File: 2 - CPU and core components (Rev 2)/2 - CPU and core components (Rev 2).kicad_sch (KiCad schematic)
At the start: 1 part

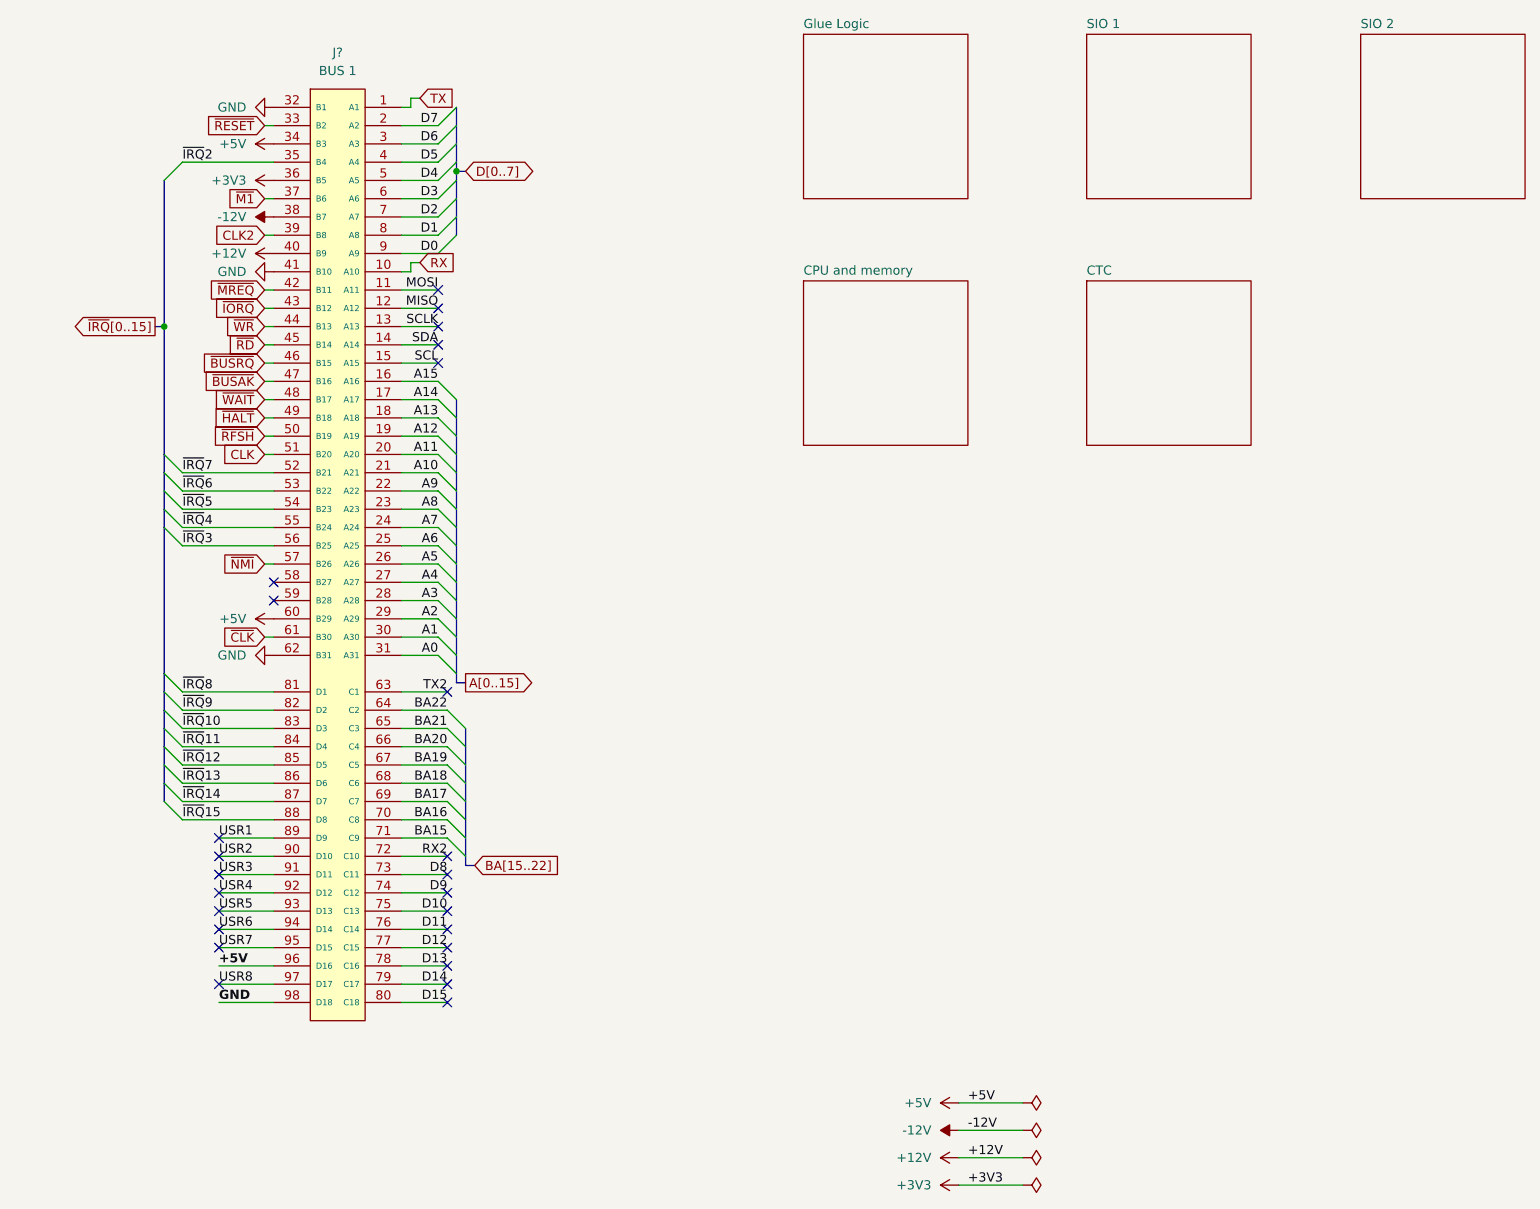
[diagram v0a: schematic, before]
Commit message: Replacing a lot of TTL chips by 2 PLDs. Also, added blinkenlights.
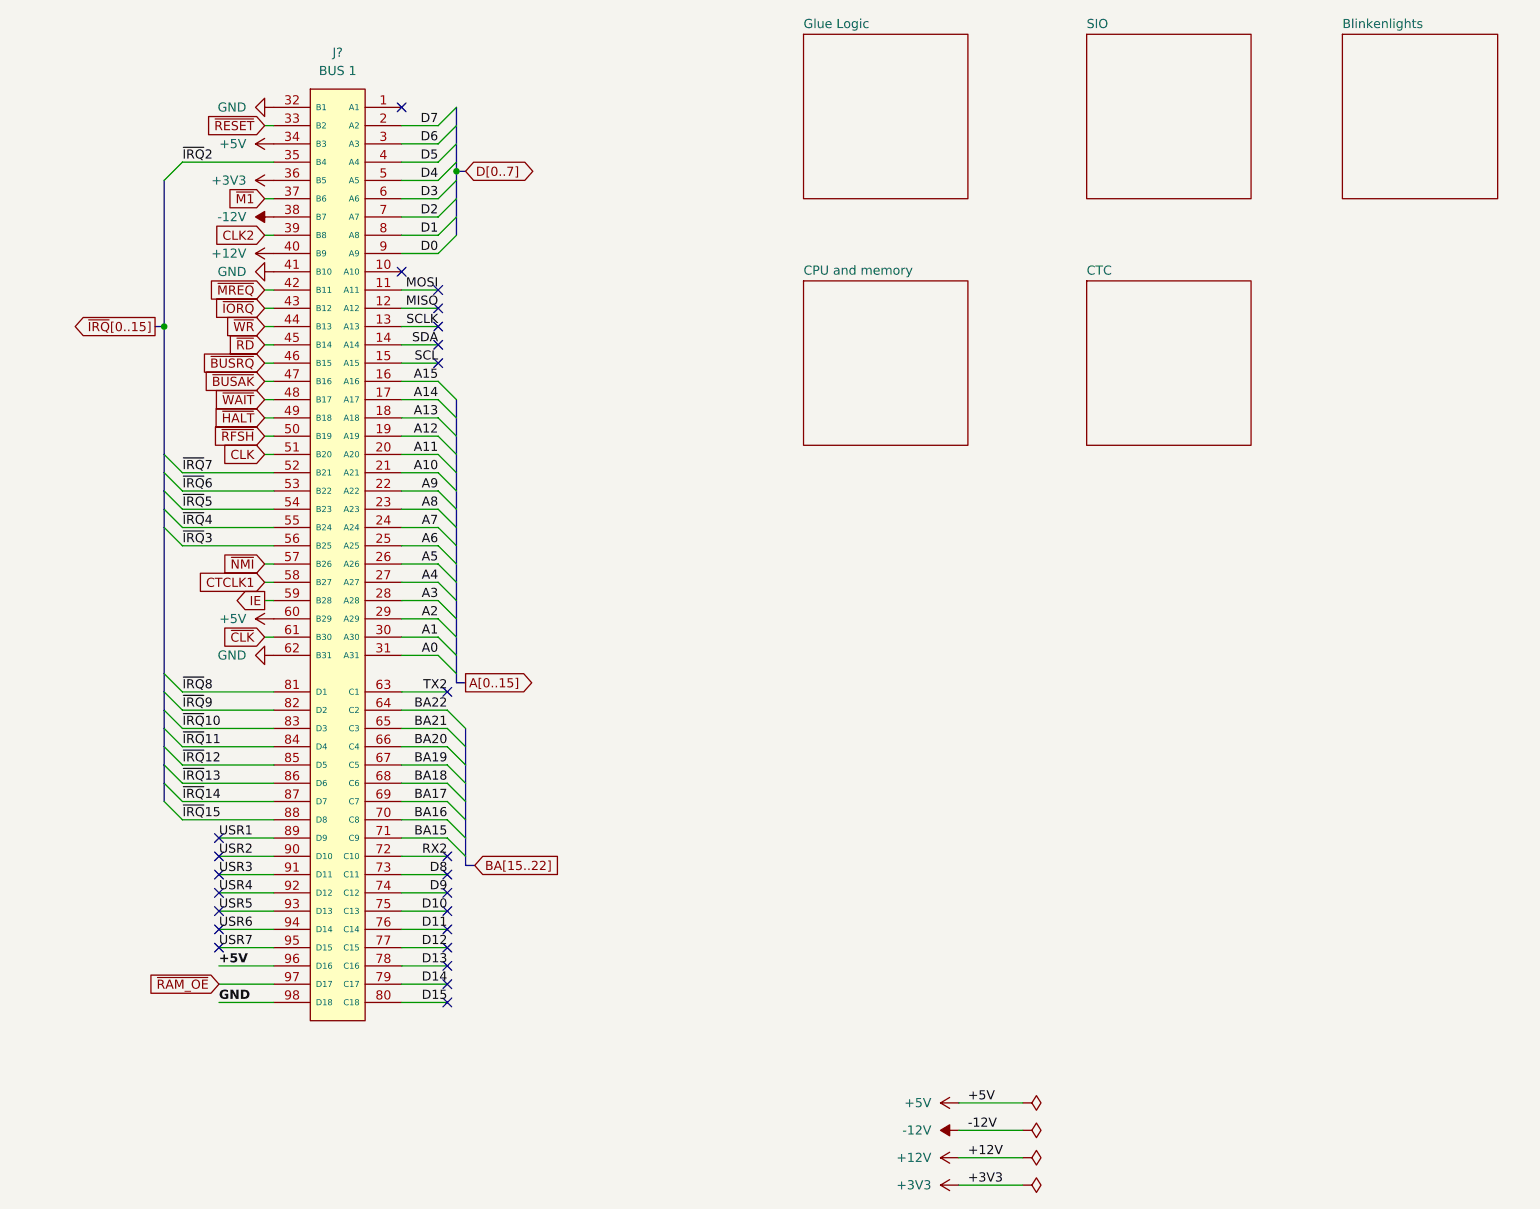
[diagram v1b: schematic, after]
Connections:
- net CTCLK1: now reaches J?.58 (B27)
- net IE: now reaches J?.59 (B28)
- net RX: no longer names the net of J?.10 (A10)
- net TX: no longer names the net of J?.1 (A1)
- net USR8 renamed ~{RAM_OE}
- no-connect marks 25 -> 24
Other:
- sheet SIO 1 renamed SIO
- removed sheet SIO 2
- added sheet Blinkenlights (Blinkenlights.kicad_sch)
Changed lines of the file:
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@@
   )
   (no_connect (at 72.39 152.4))
-  (no_connect (at 48.26 111.76))
   (no_connect (at 40.64 144.78))
   (no_connect (at 71.12 73.66))
@@
   (no_connect (at 40.64 160.02))
   (no_connect (at 40.64 152.4))
-  (no_connect (at 48.26 109.22))
   (no_connect (at 72.39 157.48))
   (no_connect (at 71.12 68.58))
   (no_connect (at 72.39 162.56))
   (no_connect (at 72.39 167.64))
+  (no_connect (at 66.04 66.04))
   (no_connect (at 71.12 76.2))
   (no_connect (at 72.39 165.1))
+  (no_connect (at 66.04 43.18))
   (no_connect (at 40.64 154.94))
   (no_connect (at 40.64 149.86))
-  (no_connect (at 40.64 165.1))
   (no_connect (at 71.12 71.12))
   (no_connect (at 40.64 157.48))
@@
     (stroke (width 0) (type default))
   )
-  (wire (pts (xy 68.58 41.91) (xy 67.31 41.91))
-    (stroke (width 0) (type default))
-  )
   (wire (pts (xy 66.04 106.68) (xy 71.12 106.68))
     (stroke (width 0) (type default))
@@
     (stroke (width 0) (type default))
   )
-  (wire (pts (xy 67.31 66.04) (xy 66.04 66.04))
-    (stroke (width 0) (type default))
-  )
   (bus (pts (xy 73.66 83.82) (xy 73.66 86.36))
     (stroke (width 0) (type default))
@@
     (stroke (width 0) (type default))
   )
-  (wire (pts (xy 67.31 64.77) (xy 68.58 64.77))
-    (stroke (width 0) (type default))
-  )
   (wire (pts (xy 143.51 189.23) (xy 152.4 189.23))
     (stroke (width 0) (type default))
@@
     (stroke (width 0) (type default))
   )
-  (wire (pts (xy 67.31 64.77) (xy 67.31 66.04))
+  (wire (pts (xy 46.99 111.76) (xy 48.26 111.76))
     (stroke (width 0) (type default))
   )
@@
     (stroke (width 0) (type default))
   )
-  (wire (pts (xy 67.31 41.91) (xy 67.31 43.18))
-    (stroke (width 0) (type default))
-  )
   (wire (pts (xy 40.64 154.94) (xy 48.26 154.94))
     (stroke (width 0) (type default))
@@
     (stroke (width 0) (type default))
   )
+  (wire (pts (xy 46.99 109.22) (xy 48.26 109.22))
+    (stroke (width 0) (type default))
+  )
   (bus (pts (xy 33.02 96.52) (xy 33.02 99.06))
     (stroke (width 0) (type default))
@@
   )
   (bus (pts (xy 33.02 99.06) (xy 33.02 101.6))
-    (stroke (width 0) (type default))
-  )
-  (wire (pts (xy 66.04 43.18) (xy 67.31 43.18))
     (stroke (width 0) (type default))
   )
@@
     (effects (font (size 1.27 1.27)) (justify right bottom))
   )
-  (label "USR8" (at 40.64 165.1 0) (fields_autoplaced)
-    (effects (font (size 1.27 1.27)) (justify left bottom))
-  )
   (label "GND" (at 40.64 167.64 0) (fields_autoplaced)
     (effects (font (size 1.27 1.27) (thickness 0.254) bold) (justify left bottom))
@@
     )
   )
-  (global_label "TX" (shape input) (at 68.58 41.91 0) (fields_autoplaced)
-    (effects (font (size 1.27 1.27)) (justify left))
-    (property "Intersheetrefs" "${INTERSHEET_REFS}" (at 73.7423 41.91 0)
-      (effects (font (size 1.27 1.27)) (justify left) hide)
-    )
-  )
   (global_label "CLK2" (shape input) (at 46.99 60.96 180) (fields_autoplaced)
     (effects (font (size 1.27 1.27)) (justify right))
     (property "Intersheetrefs" "${INTERSHEET_REFS}" (at 39.2272 60.96 0)
       (effects (font (size 1.27 1.27)) (justify right) hide)
-    )
-  )
-  (global_label "RX" (shape input) (at 68.58 64.77 0) (fields_autoplaced)
-    (effects (font (size 1.27 1.27)) (justify left))
-    (property "Intersheetrefs" "${INTERSHEET_REFS}" (at 74.0447 64.77 0)
-      (effects (font (size 1.27 1.27)) (justify left) hide)
     )
   )
@@
     )
   )
+  (global_label "CTCLK1" (shape input) (at 46.99 109.22 180) (fields_autoplaced)
+    (effects (font (size 1.27 1.27)) (justify right))
+    (property "Intersheetrefs" "${INTERSHEET_REFS}" (at 36.9896 109.22 0)
+      (effects (font (size 1.27 1.27)) (justify right) hide)
+    )
+  )
+  (global_label "IE" (shape output) (at 46.99 111.76 180) (fields_autoplaced)
+    (effects (font (size 1.27 1.27)) (justify right))
+    (property "Intersheetrefs" "${INTERSHEET_REFS}" (at 42.251 111.76 0)
+      (effects (font (size 1.27 1.27)) (justify right) hide)
+    )
+  )
   (global_label "~{IORQ}" (shape input) (at 46.99 71.12 180) (fields_autoplaced)
     (effects (font (size 1.27 1.27)) (justify right))
     (property "Intersheetrefs" "${INTERSHEET_REFS}" (at 39.469 71.12 0)
+      (effects (font (size 1.27 1.27)) (justify right) hide)
+    )
+  )
+  (global_label "~{RAM_OE}" (shape input) (at 40.64 165.1 180) (fields_autoplaced)
+    (effects (font (size 1.27 1.27)) (justify right))
+    (property "Intersheetrefs" "${INTERSHEET_REFS}" (at 30.3977 165.1 0)
       (effects (font (size 1.27 1.27)) (justify right) hide)
     )
@@
   (symbol (lib_id "power:GND") (at 48.26 119.38 270) (mirror x) (unit 1)
     (in_bom yes) (on_board yes) (dnp no) (fields_autoplaced)
-    (property "Reference" "#PWR034" (at 41.91 119.38 0)
+    (property "Reference" "#PWR040" (at 41.91 119.38 0)
       (effects (font (size 1.27 1.27)) hide)
     )
@@
       (project "2 - CPU and core components (Rev 2)"
         (path "/fc5c05aa-044e-4225-a29e-03b20eedf682"
-          (reference "#PWR034") (unit 1)
+          (reference "#PWR040") (unit 1)
         )
       )
@@
       (project "2 - CPU and core components (Rev 2)"
         (path "/fc5c05aa-044e-4225-a29e-03b20eedf682"
-          (reference "#PWR033") (unit 1)
+          (reference "#PWR039") (unit 1)
         )
       )
@@
   (symbol (lib_id "power:GND") (at 48.26 66.04 270) (unit 1)
     (in_bom yes) (on_board yes) (dnp no) (fields_autoplaced)
-    (property "Reference" "#PWR032" (at 41.91 66.04 0)
+    (property "Reference" "#PWR038" (at 41.91 66.04 0)
       (effects (font (size 1.27 1.27)) hide)
     )
@@
       (project "2 - CPU and core components (Rev 2)"
         (path "/fc5c05aa-044e-4225-a29e-03b20eedf682"
-          (reference "#PWR032") (unit 1)
+          (reference "#PWR038") (unit 1)
         )
       )
@@
       (project "2 - CPU and core components (Rev 2)"
         (path "/fc5c05aa-044e-4225-a29e-03b20eedf682"
-          (reference "#PWR031") (unit 1)
+          (reference "#PWR037") (unit 1)
         )
       )
@@
       (project "2 - CPU and core components (Rev 2)"
         (path "/fc5c05aa-044e-4225-a29e-03b20eedf682"
-          (reference "#PWR028") (unit 1)
+          (reference "#PWR034") (unit 1)
         )
       )
@@
       (project "2 - CPU and core components (Rev 2)"
         (path "/fc5c05aa-044e-4225-a29e-03b20eedf682"
-          (reference "#PWR038") (unit 1)
+          (reference "#PWR044") (unit 1)
         )
       )
@@
       (project "2 - CPU and core components (Rev 2)"
         (path "/fc5c05aa-044e-4225-a29e-03b20eedf682"
-          (reference "#PWR036") (unit 1)
+          (reference "#PWR042") (unit 1)
         )
       )
@@
       (project "2 - CPU and core components (Rev 2)"
         (path "/fc5c05aa-044e-4225-a29e-03b20eedf682"
-          (reference "#PWR030") (unit 1)
+          (reference "#PWR036") (unit 1)
         )
       )
@@
   (symbol (lib_id "power:GND") (at 48.26 43.18 270) (unit 1)
     (in_bom yes) (on_board yes) (dnp no) (fields_autoplaced)
-    (property "Reference" "#PWR027" (at 41.91 43.18 0)
+    (property "Reference" "#PWR033" (at 41.91 43.18 0)
       (effects (font (size 1.27 1.27)) hide)
     )
@@
       (project "2 - CPU and core components (Rev 2)"
         (path "/fc5c05aa-044e-4225-a29e-03b20eedf682"
-          (reference "#PWR027") (unit 1)
+          (reference "#PWR033") (unit 1)
         )
       )
@@
       (project "2 - CPU and core components (Rev 2)"
         (path "/fc5c05aa-044e-4225-a29e-03b20eedf682"
-          (reference "#PWR037") (unit 1)
+          (reference "#PWR043") (unit 1)
         )
       )
@@
       (project "2 - CPU and core components (Rev 2)"
         (path "/fc5c05aa-044e-4225-a29e-03b20eedf682"
-          (reference "#PWR035") (unit 1)
+          (reference "#PWR041") (unit 1)
         )
       )
@@
       (project "2 - CPU and core components (Rev 2)"
         (path "/fc5c05aa-044e-4225-a29e-03b20eedf682"
-          (reference "#PWR029") (unit 1)
+          (reference "#PWR035") (unit 1)
         )
       )
@@
     (stroke (width 0.1524) (type solid))
     (fill (color 0 0 0 0.0000))
-    (property "Sheetname" "SIO 1" (at 161.29 32.3084 0)
+    (property "Sheetname" "SIO" (at 161.29 32.3084 0)
       (effects (font (size 1.27 1.27)) (justify left bottom))
     )
@@
     )
   )
-  (sheet (at 199.39 33.02) (size 22.86 22.86) (fields_autoplaced)
+  (sheet (at 196.85 33.02) (size 21.59 22.86) (fields_autoplaced)
     (stroke (width 0.1524) (type solid))
     (fill (color 0 0 0 0.0000))
-    (property "Sheetname" "SIO 2" (at 199.39 32.3084 0)
+    (property "Sheetname" "Blinkenlights" (at 196.85 32.3084 0)
       (effects (font (size 1.27 1.27)) (justify left bottom))
     )
-    (property "Sheetfile" "SIO2.kicad_sch" (at 199.39 56.4646 0)
+    (property "Sheetfile" "Blinkenlights.kicad_sch" (at 196.85 56.4646 0)
       (effects (font (size 1.27 1.27)) (justify left top) hide)
     )
